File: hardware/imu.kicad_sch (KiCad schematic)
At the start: 5 parts, among them U11 BMI270, U12 TPS7A2018

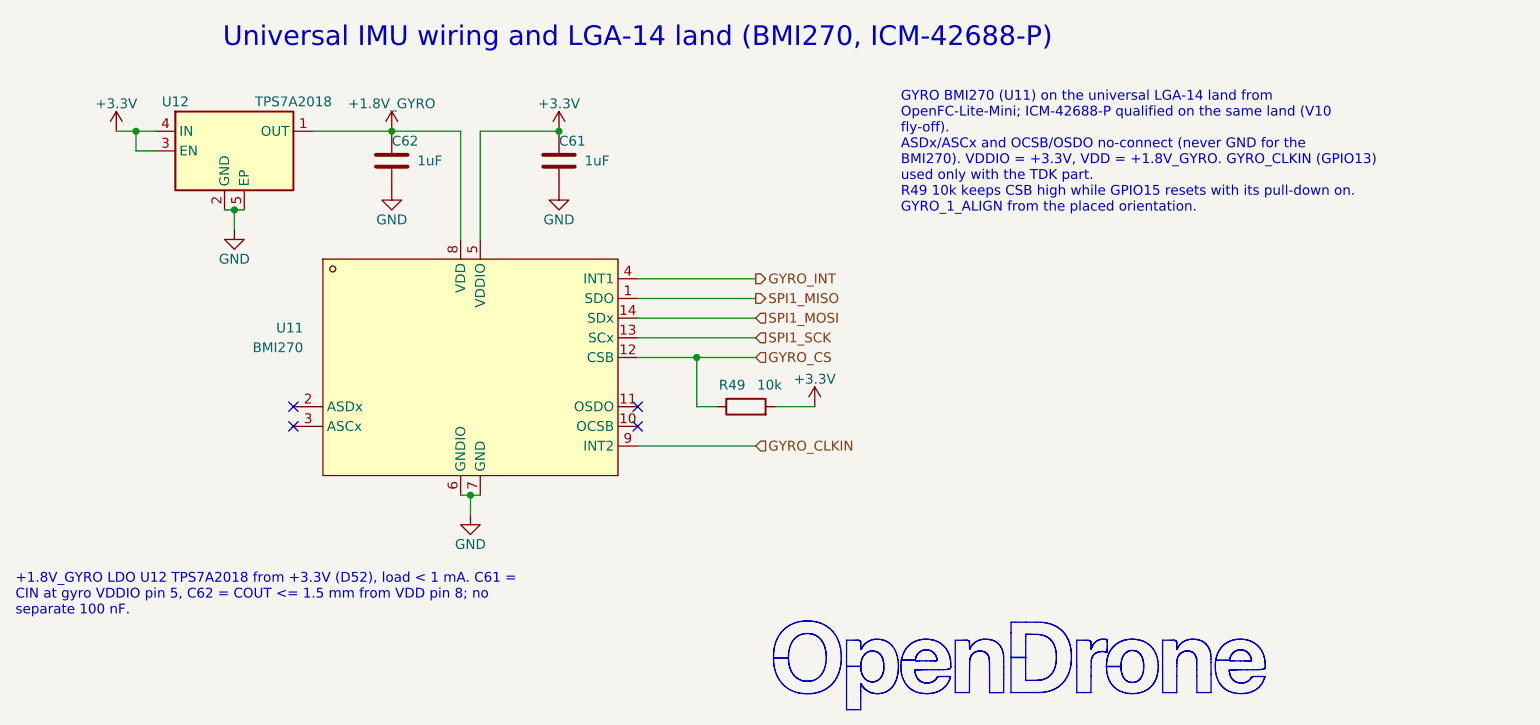
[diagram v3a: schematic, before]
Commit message: Footprint audit vs datasheets, 0201 lands to Murata minimum, schematic notes shortened
Footprints: 45 checked against their datasheets by group, no pin or
land errors. C/R/L_0201_..._L pad height 0.28 -> 0.30 (Murata GRM03
reflow table c >= 0.30); other lands already at least density per D109
and left unchanged. Land spec texts cleaned (sources, shared parts).

Schematic notes: 157 -> 152 items, 19.5k -> 9.7k characters, all
current (diode-OR, removed parts, RTC6705 filters, TX0/RX0).

check_footprint 107/107 lib specs PASS; ERC 0 errors / 2 warnings;
check_netlist 7 ok; sch_integrate --check clean. Board not synced.

Co-Authored-By: Claude Opus 5.5 <noreply@anthropic.com>
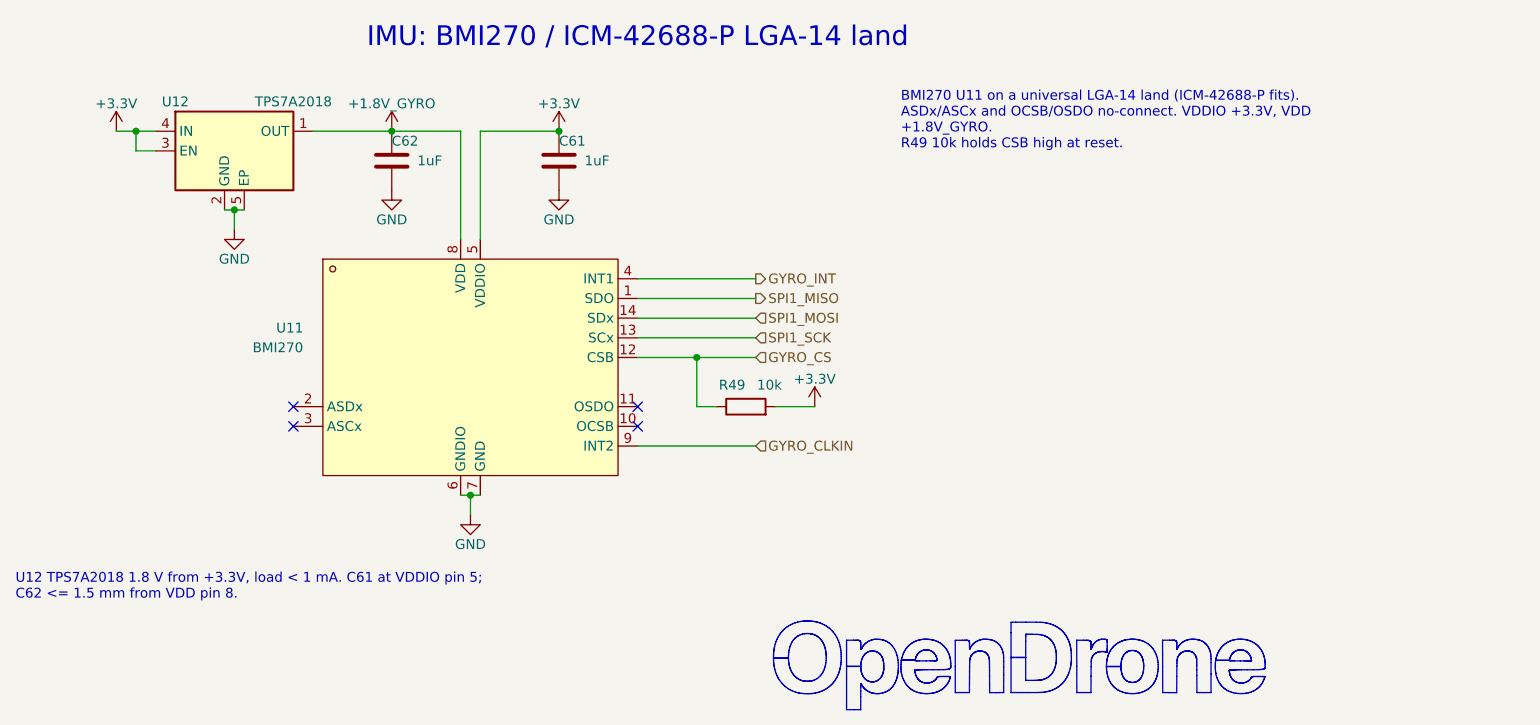
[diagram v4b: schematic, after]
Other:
- note added: "IMU: BMI270 / ICM-42688-P LGA-14 land"
- note removed: "Universal IMU wiring and LGA-14 land (BMI270, ICM-42688-P)"
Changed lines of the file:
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@@
 		)
 	)
-	(text "Universal IMU wiring and LGA-14 land (BMI270, ICM-42688-P)"
+	(text "IMU: BMI270 / ICM-42688-P LGA-14 land"
 		(exclude_from_sim no)
 		(at 93.98 31.115 0)
@@
 		)
 	)
-	(text_box "GYRO BMI270 (U11) on the universal LGA-14 land from OpenFC-Lite-Mini; ICM-42688-P qualified on the same land (V10 fly-off).\nASDx/ASCx and OCSB/OSDO no-connect (never GND for the BMI270). VDDIO = +3.3V, VDD = +1.8V_GYRO. GYRO_CLKIN (GPIO13) used only with the TDK part.\nR49 10k keeps CSB high while GPIO15 resets with its pull-down on. GYRO_1_ALIGN from the placed orientation."
+	(text_box "BMI270 U11 on a universal LGA-14 land (ICM-42688-P fits). ASDx/ASCx and OCSB/OSDO no-connect. VDDIO +3.3V, VDD +1.8V_GYRO.\nR49 10k holds CSB high at reset."
 		(exclude_from_sim no)
 		(at 127 36.83 0)
@@
 		)
 	)
-	(text_box "+1.8V_GYRO LDO U12 TPS7A2018 from +3.3V (D52), load < 1 mA. C61 = CIN at gyro VDDIO pin 5, C62 = COUT <= 1.5 mm from VDD pin 8; no separate 100 nF."
+	(text_box "U12 TPS7A2018 1.8 V from +3.3V, load < 1 mA. C61 at VDDIO pin 5; C62 <= 1.5 mm from VDD pin 8."
 		(exclude_from_sim no)
 		(at 12.7 99.06 0)
